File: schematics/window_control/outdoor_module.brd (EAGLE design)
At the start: 47 x 56.8 mm, 23 parts, among them J10 USBASP_PIN, J4 JST-XH2.54-3P, U5 BMP280 5V module, U6 LM317L, U7 LM358, U8 ATMEGA328P, U9 GY-SGP30

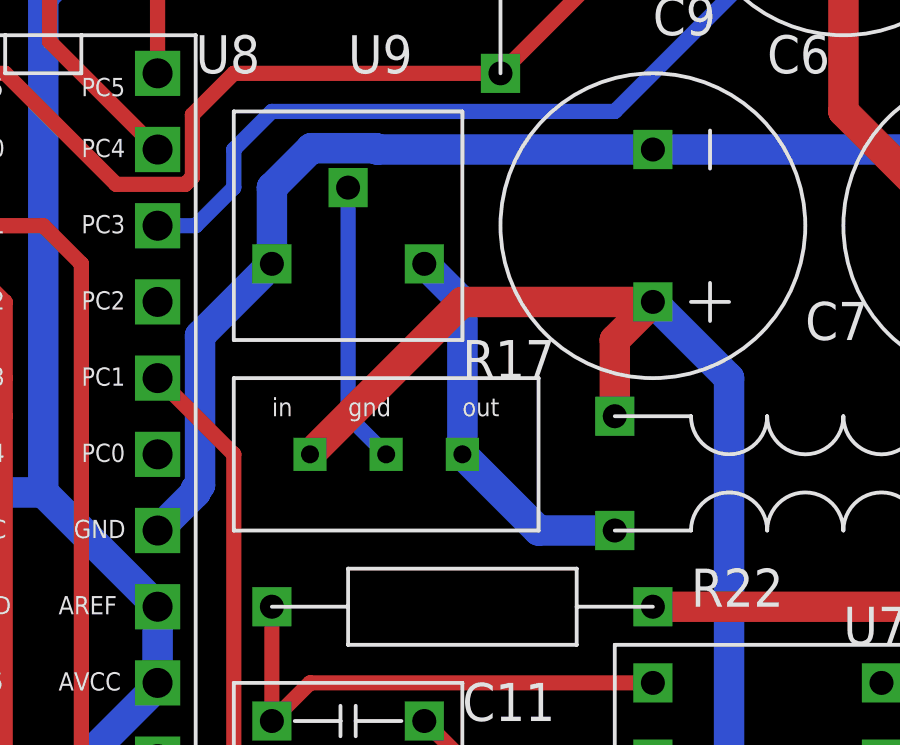
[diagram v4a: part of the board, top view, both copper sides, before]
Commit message: fixed error in outdoor board and schema
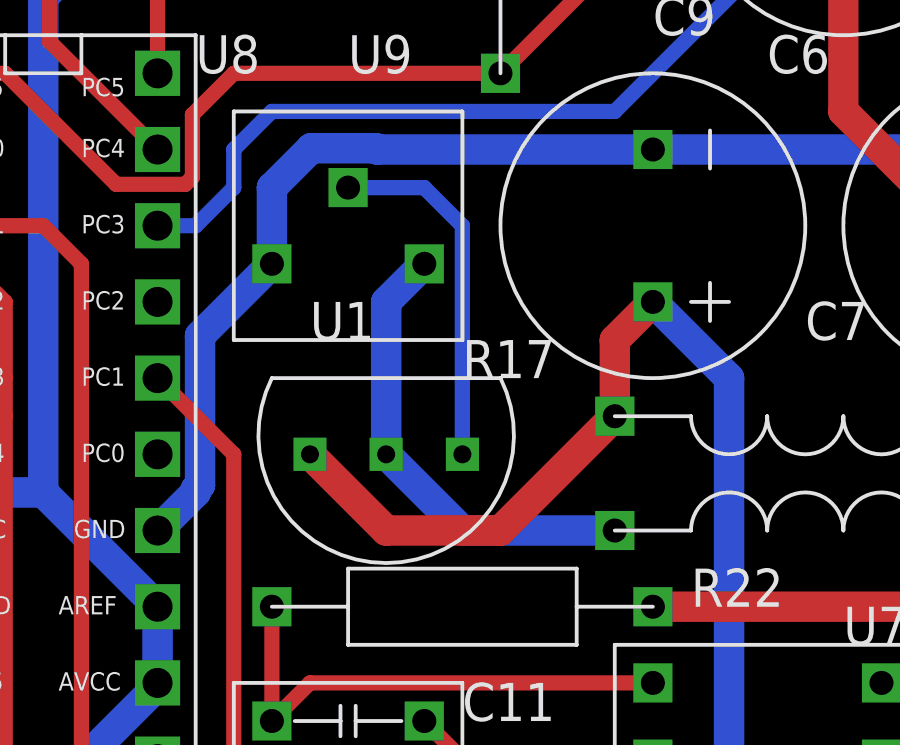
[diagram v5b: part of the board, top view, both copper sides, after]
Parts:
- removed U6: LM317L, my_devices:VOLTAGE_REGULATOR
- added U1: LM317L, my_devices:TO-92
- R17: value 10K -> 2K
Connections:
- net N$17: now also U1.P3; no longer U6.GND
- net OUT: now also U1.P2; no longer U6.OUT
- net OUTDOOR_+5V_F: now also U1.P1; no longer U6.IN
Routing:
- net OUT: track 13.0 -> 15.5 mm
- net N$17: track 9.42 -> 12.0 mm
- net OUTDOOR_+5V_F: track 44.8 -> 44.1 mm
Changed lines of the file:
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@@
 <element name="L2" library="my_devices" package="L-EC24" value="EC24-561K, 560 uH" x="121.92" y="3.81" smashed="yes" rot="R180"/>
 <element name="L3" library="my_devices" package="L-EC24" value="EC24-561K, 560 uH" x="121.92" y="0" smashed="yes"/>
-<element name="R17" library="my_devices" package="RD-3362H" value="10K" x="105.41" y="10.16" smashed="yes"/>
+<element name="R17" library="my_devices" package="RD-3362H" value="2K" x="105.41" y="10.16" smashed="yes"/>
 <element name="R18" library="my_devices" package="R" value="3K" x="121.92" y="-16.51" smashed="yes">
 <attribute name="R" value="" x="161.29" y="-76.2" size="1.778" layer="27" display="off"/>
@@
 <element name="R23" library="my_devices" package="RD-3296Z" value="200K" x="102.87" y="-13.97" smashed="yes" rot="R270"/>
 <element name="U5" library="my_devices" package="BME280-CONNECTOR-ONLY" value="BMP280 5V module" x="91.44" y="22.86" smashed="yes" rot="R180"/>
-<element name="U6" library="my_devices" package="VOLTAGE_REGULATOR" value="LM317L" x="106.68" y="2.54" smashed="yes"/>
 <element name="U7" library="my_devices" package="DIP8" value="LM358" x="119.38" y="-8.89" smashed="yes" rot="R180"/>
 <element name="U8" library="my_devices" package="ATMEGA328P" value="ATMEGA328P" x="95.25" y="0" smashed="yes"/>
@@
 <element name="J4" library="my_devices" package="JST-XH254-3P" value="JST-XH2.54-3P" x="130.81" y="21.59" smashed="yes" rot="R90">
 <attribute name="NAME" x="133.35" y="15.24" size="1.27" layer="21" rot="R180"/>
+</element>
+<element name="U1" library="my_devices" package="TO-92" value="LM317L" x="106.68" y="2.54" smashed="yes">
+<attribute name="NAME" x="104.14" y="6.35" size="1.27" layer="21"/>
 </element>
 </elements>
@@
 <wire x1="124.46" y1="-11.43" x2="123.19" y2="-10.16" width="0.508" layer="1"/>
 </signal>
-<signal name="OUT">
-<contactref element="U6" pad="OUT"/>
-<contactref element="L3" pad="P$1"/>
-<contactref element="R17" pad="P2"/>
-<wire x1="107.95" y1="8.89" x2="109.22" y2="7.62" width="1.016" layer="16"/>
-<wire x1="109.22" y1="7.62" x2="109.22" y2="2.54" width="1.016" layer="16"/>
-<wire x1="109.22" y1="2.54" x2="111.76" y2="0" width="1.016" layer="16"/>
-<wire x1="111.76" y1="0" x2="114.3" y2="0" width="1.016" layer="16"/>
-</signal>
 <signal name="OUTDOOR_DATA_OUT">
 <contactref element="U8" pad="PC3"/>
@@
 </signal>
 <signal name="N$17">
-<contactref element="U6" pad="GND"/>
 <contactref element="R17" pad="P3"/>
-<wire x1="106.68" y1="2.54" x2="105.41" y2="3.81" width="0.508" layer="16"/>
-<wire x1="105.41" y1="3.81" x2="105.41" y2="11.43" width="0.508" layer="16"/>
+<contactref element="U1" pad="P3"/>
+<wire x1="105.41" y1="11.43" x2="107.95" y2="11.43" width="0.508" layer="16"/>
+<wire x1="107.95" y1="11.43" x2="109.22" y2="10.16" width="0.508" layer="16"/>
+<wire x1="109.22" y1="10.16" x2="109.22" y2="2.54" width="0.508" layer="16"/>
 </signal>
 <signal name="N$18">
@@
 <contactref element="L2" pad="P$2"/>
 <contactref element="C7" pad="PIN_PLUS"/>
-<contactref element="U6" pad="IN"/>
 <contactref element="R18" pad="P$1"/>
 <contactref element="U7" pad="PIN_8"/>
@@
 <wire x1="114.3" y1="3.81" x2="114.3" y2="6.35" width="1.016" layer="1"/>
 <wire x1="114.3" y1="6.35" x2="115.57" y2="7.62" width="1.016" layer="1"/>
-<wire x1="109.22" y1="7.62" x2="104.14" y2="2.54" width="1.016" layer="1"/>
-<wire x1="115.57" y1="7.62" x2="109.22" y2="7.62" width="1.016" layer="1"/>
 <wire x1="118.11" y1="5.08" x2="115.57" y2="7.62" width="1.016" layer="16"/>
 <wire x1="118.11" y1="-11.43" x2="118.11" y2="5.08" width="1.016" layer="16"/>
+<contactref element="U1" pad="P1"/>
+<wire x1="114.3" y1="3.81" x2="110.49" y2="0" width="1.016" layer="1"/>
+<wire x1="106.68" y1="0" x2="104.14" y2="2.54" width="1.016" layer="1"/>
+<wire x1="110.49" y1="0" x2="106.68" y2="0" width="1.016" layer="1"/>
 </signal>
 <signal name="N$24">
@@
 <wire x1="96.52" y1="-21.59" x2="96.52" y2="8.89" width="0.508" layer="1"/>
 </signal>
+<signal name="OUT">
+<contactref element="L3" pad="P$1"/>
+<contactref element="R17" pad="P2"/>
+<contactref element="U1" pad="P2"/>
+<wire x1="106.68" y1="2.54" x2="109.22" y2="0" width="1.016" layer="16"/>
+<wire x1="109.22" y1="0" x2="114.3" y2="0" width="1.016" layer="16"/>
+<wire x1="107.95" y1="8.89" x2="106.68" y2="7.62" width="1.016" layer="16"/>
+<wire x1="106.68" y1="7.62" x2="106.68" y2="2.54" width="1.016" layer="16"/>
+</signal>
 </signals>

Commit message: actualized voltage regulator nominal
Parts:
- U1: value LM317L -> LM317LZ-TR
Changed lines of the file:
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@@
 <attribute name="NAME" x="133.35" y="15.24" size="1.27" layer="21" rot="R180"/>
 </element>
-<element name="U1" library="my_devices" package="TO-92" value="LM317L" x="106.68" y="2.54" smashed="yes">
+<element name="U1" library="my_devices" package="TO-92" value="LM317LZ-TR" x="106.68" y="2.54" smashed="yes">
 <attribute name="NAME" x="104.14" y="6.35" size="1.27" layer="21"/>
 </element>
